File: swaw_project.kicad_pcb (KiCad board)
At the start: 2 copper layers, 68.6 x 53.3 mm, 22 parts, among them P1 Power, P2 Analog, P3 Digital, P4 Digital, P5 CONN_01X01, P6 CONN_01X01, P7 CONN_01X01, P8 CONN_01X01, Q1 2N7000, Q2 2N7000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

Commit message: First version of layout
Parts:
- moved R2 2.54 mm to (128.3, 94.6), turned to 0 degrees
- moved C4 1.78 mm to (135.8, 99.3)
- moved R5 0.43 mm to (135.1, 80.6), turned to 180 degrees
- moved C3 0.42 mm to (128.8, 108.2)
- moved R1 0.41 mm to (134.3, 94.6)
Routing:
- net +5V: track 0.00 -> 143.2 mm
- net GND: track 0.00 -> 122.4 mm, vias 0 -> 9
- net +3V3: track 0.00 -> 95.2 mm, vias 0 -> 6
- net /0(Rx): track 0.00 -> 25.1 mm
- net /1(Tx): track 0.00 -> 15.2 mm
- net /A5(SCL): track 0.00 -> 12.9 mm
- net Net-(HC-05_PIO1-Pad3): track 0.00 -> 12.8 mm
- net Net-(Q2-Pad1): track 0.00 -> 12.6 mm, vias 0 -> 1
- net /A4(SDA): track 0.00 -> 12.6 mm
- net Net-(Q1-Pad1): track 0.00 -> 12.4 mm, vias 0 -> 1
- net Net-(C4-Pad1): track 0.00 -> 7.66 mm, vias 0 -> 1
- net Net-(C3-Pad1): track 0.00 -> 3.93 mm, vias 0 -> 1

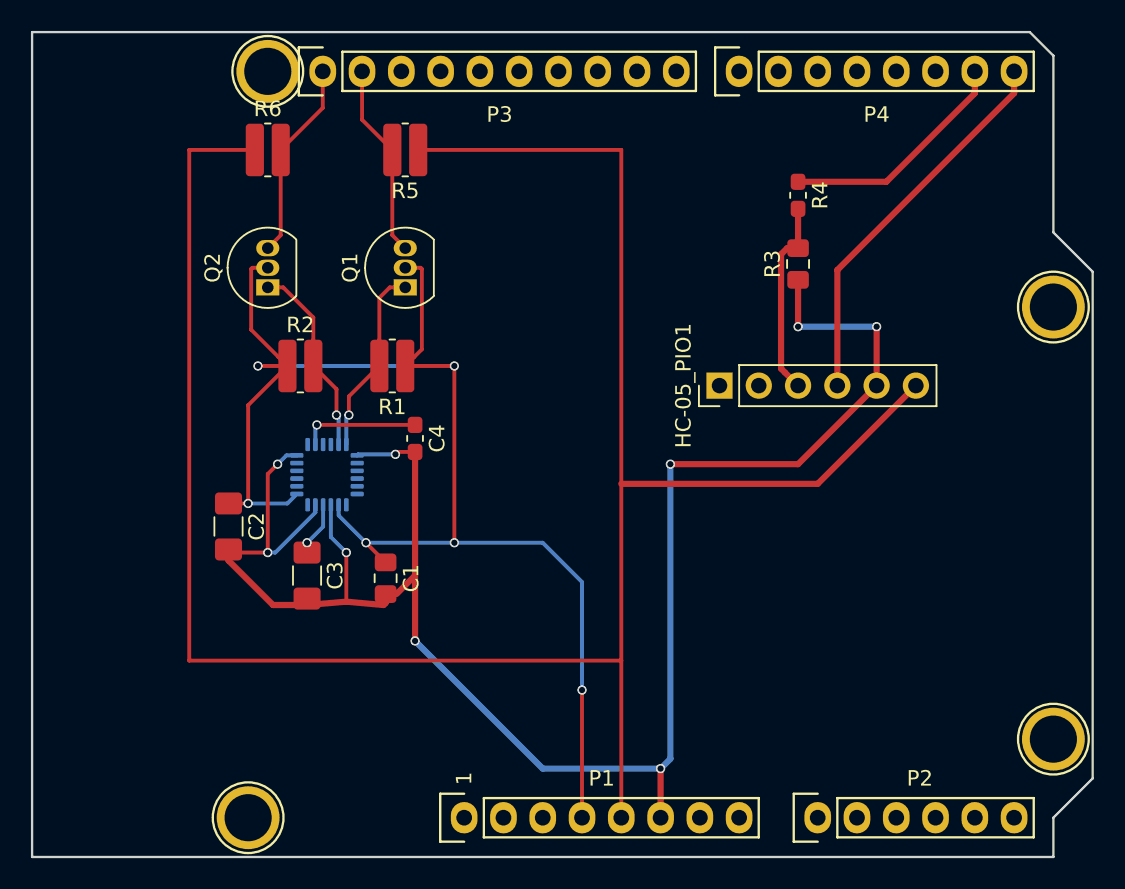
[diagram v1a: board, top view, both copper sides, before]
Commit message: Add files via upload
Removing right angles for paths
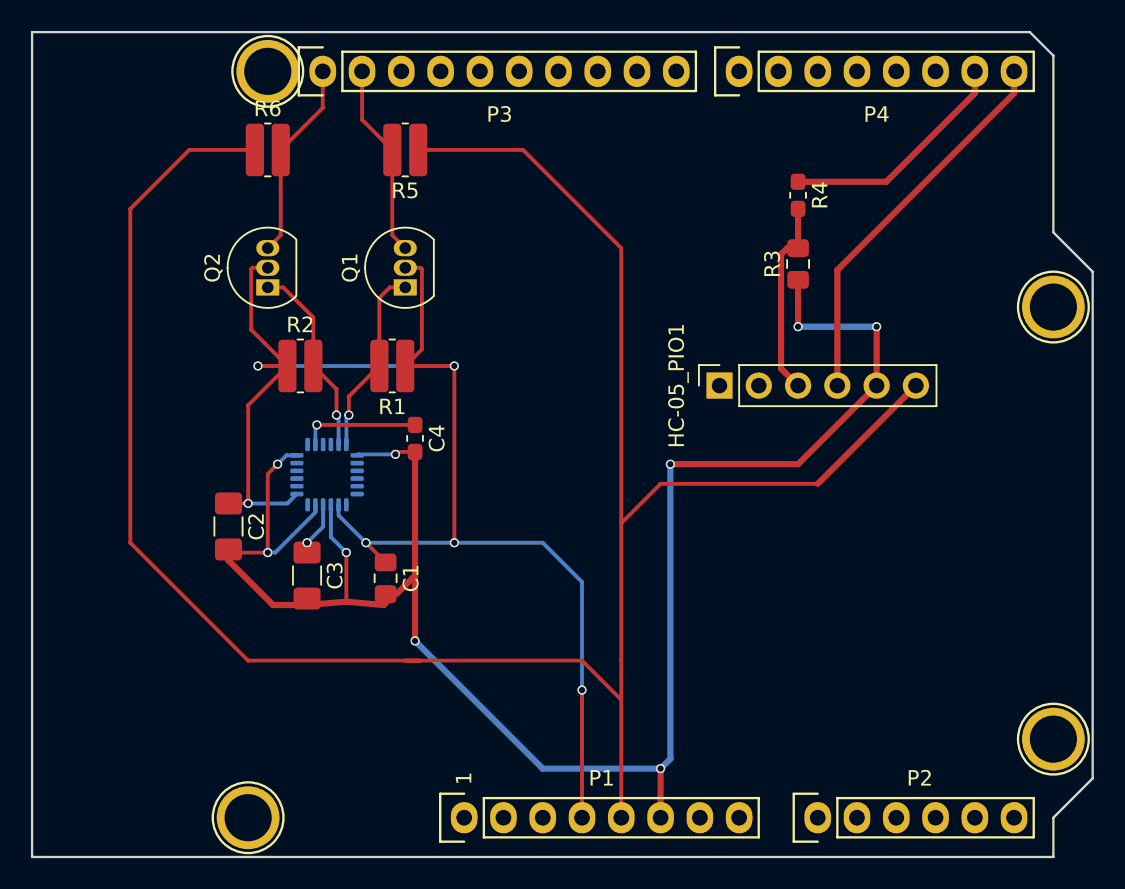
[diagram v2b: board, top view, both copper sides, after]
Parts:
- HC-05_PIO1: footprint Connector_PinHeader_2.54mm:PinHeader_1x06_P2.54mm_Vertical -> Connector_PinSocket_2.54mm:PinSocket_1x06_P2.54mm_Vertical
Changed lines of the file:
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@@
-(kicad_pcb (version 20171130) (host pcbnew 5.1.5)
+(kicad_pcb (version 20171130) (host pcbnew "(5.1.5)-3")
   (general
     (thickness 1.6)
     (drawings 27)
-    (tracks 135)
+    (tracks 142)
     (zones 0)
     (modules 22)
@@
   )
   (setup
-    (last_trace_width 0.4)
+    (last_trace_width 0.25)
     (user_trace_width 0.2)
     (user_trace_width 0.4)
@@
     (aux_axis_origin 110.998 126.365)
     (grid_origin 110.998 126.365)
-    (visible_elements FFFFFF7F)
+    (visible_elements 7FFFFFFF)
     (pcbplotparams
       (layerselection 0x00030_80000001)
@@
     (add_net "Net-(U1-Pad7)")
   )
+  (module Connector_PinSocket_2.54mm:PinSocket_1x06_P2.54mm_Vertical (layer F.Cu)
+    (at 155.448 95.885 90)
+    (descr "Through hole straight socket strip, 1x06, 2.54mm pitch, single row (from Kicad 4.0.7), script generated")
+    (tags "Through hole socket strip THT 1x06 2.54mm single row")
+    (fp_text reference HC-05_PIO1 (at 0 -2.77 90) (layer F.SilkS)
+      (effects (font (size 1 1) (thickness 0.15)))
+    )
+    (fp_text value Bluetooh_PIO (at 0 15.47 90) (layer F.Fab)
+      (effects (font (size 1 1) (thickness 0.15)))
+    )
+    (fp_text user %R (at 0 6.35) (layer F.Fab)
+      (effects (font (size 1 1) (thickness 0.15)))
+    )
+    (fp_line (start -1.8 14.45) (end -1.8 -1.8) (layer F.CrtYd) (width 0.05))
+    (fp_line (start 1.75 14.45) (end -1.8 14.45) (layer F.CrtYd) (width 0.05))
+    (fp_line (start 1.75 -1.8) (end 1.75 14.45) (layer F.CrtYd) (width 0.05))
+    (fp_line (start -1.8 -1.8) (end 1.75 -1.8) (layer F.CrtYd) (width 0.05))
+    (fp_line (start 0 -1.33) (end 1.33 -1.33) (layer F.SilkS) (width 0.12))
+    (fp_line (start 1.33 -1.33) (end 1.33 0) (layer F.SilkS) (width 0.12))
+    (fp_line (start 1.33 1.27) (end 1.33 14.03) (layer F.SilkS) (width 0.12))
+    (fp_line (start -1.33 14.03) (end 1.33 14.03) (layer F.SilkS) (width 0.12))
+    (fp_line (start -1.33 1.27) (end -1.33 14.03) (layer F.SilkS) (width 0.12))
+    (fp_line (start -1.33 1.27) (end 1.33 1.27) (layer F.SilkS) (width 0.12))
+    (fp_line (start -1.27 13.97) (end -1.27 -1.27) (layer F.Fab) (width 0.1))
+    (fp_line (start 1.27 13.97) (end -1.27 13.97) (layer F.Fab) (width 0.1))
+    (fp_line (start 1.27 -0.635) (end 1.27 13.97) (layer F.Fab) (width 0.1))
+    (fp_line (start 0.635 -1.27) (end 1.27 -0.635) (layer F.Fab) (width 0.1))
+    (fp_line (start -1.27 -1.27) (end 0.635 -1.27) (layer F.Fab) (width 0.1))
+    (pad 6 thru_hole oval (at 0 12.7 90) (size 1.7 1.7) (drill 1) (layers *.Cu *.Mask)
+      (net 3 +5V))
+    (pad 5 thru_hole oval (at 0 10.16 90) (size 1.7 1.7) (drill 1) (layers *.Cu *.Mask)
+      (net 4 GND))
+    (pad 4 thru_hole oval (at 0 7.62 90) (size 1.7 1.7) (drill 1) (layers *.Cu *.Mask)
+      (net 22 "/0(Rx)"))
+    (pad 3 thru_hole oval (at 0 5.08 90) (size 1.7 1.7) (drill 1) (layers *.Cu *.Mask)
+      (net 37 "Net-(HC-05_PIO1-Pad3)"))
+    (pad 2 thru_hole oval (at 0 2.54 90) (size 1.7 1.7) (drill 1) (layers *.Cu *.Mask)
+      (net 36 "Net-(HC-05_PIO1-Pad2)"))
+    (pad 1 thru_hole rect (at 0 0 90) (size 1.7 1.7) (drill 1) (layers *.Cu *.Mask)
+      (net 35 "Net-(HC-05_PIO1-Pad1)"))
+    (model ${KISYS3DMOD}/Connector_PinSocket_2.54mm.3dshapes/PinSocket_1x06_P2.54mm_Vertical.wrl
+      (at (xyz 0 0 0))
+      (scale (xyz 1 1 1))
+      (rotate (xyz 0 0 0))
+    )
+  )
   (module Socket_Arduino_Uno:Socket_Strip_Arduino_1x08 locked (layer F.Cu)
     (at 138.938 123.825)
@@
       (net 4 GND))
     (model ${KISYS3DMOD}/Capacitor_SMD.3dshapes/C_0603_1608Metric.wrl
-      (at (xyz 0 0 0))
-      (scale (xyz 1 1 1))
-      (rotate (xyz 0 0 0))
-    )
-  )
-  (module Connector_PinHeader_2.54mm:PinHeader_1x06_P2.54mm_Vertical (layer F.Cu)
-    (at 155.448 95.885 90)
-    (descr "Through hole straight pin header, 1x06, 2.54mm pitch, single row")
-    (tags "Through hole pin header THT 1x06 2.54mm single row")
-    (fp_text reference HC-05_PIO1 (at 0 -2.33 90) (layer F.SilkS)
-      (effects (font (size 1 1) (thickness 0.15)))
-    )
-    (fp_text value Bluetooh_PIO (at 0 15.03 90) (layer F.Fab)
-      (effects (font (size 1 1) (thickness 0.15)))
-    )
-    (fp_line (start -0.635 -1.27) (end 1.27 -1.27) (layer F.Fab) (width 0.1))
-    (fp_line (start 1.27 -1.27) (end 1.27 13.97) (layer F.Fab) (width 0.1))
-    (fp_line (start 1.27 13.97) (end -1.27 13.97) (layer F.Fab) (width 0.1))
-    (fp_line (start -1.27 13.97) (end -1.27 -0.635) (layer F.Fab) (width 0.1))
-    (fp_line (start -1.27 -0.635) (end -0.635 -1.27) (layer F.Fab) (width 0.1))
-    (fp_line (start -1.33 14.03) (end 1.33 14.03) (layer F.SilkS) (width 0.12))
-    (fp_line (start -1.33 1.27) (end -1.33 14.03) (layer F.SilkS) (width 0.12))
-    (fp_line (start 1.33 1.27) (end 1.33 14.03) (layer F.SilkS) (width 0.12))
-    (fp_line (start -1.33 1.27) (end 1.33 1.27) (layer F.SilkS) (width 0.12))
-    (fp_line (start -1.33 0) (end -1.33 -1.33) (layer F.SilkS) (width 0.12))
-    (fp_line (start -1.33 -1.33) (end 0 -1.33) (layer F.SilkS) (width 0.12))
-    (fp_line (start -1.8 -1.8) (end -1.8 14.5) (layer F.CrtYd) (width 0.05))
-    (fp_line (start -1.8 14.5) (end 1.8 14.5) (layer F.CrtYd) (width 0.05))
-    (fp_line (start 1.8 14.5) (end 1.8 -1.8) (layer F.CrtYd) (width 0.05))
-    (fp_line (start 1.8 -1.8) (end -1.8 -1.8) (layer F.CrtYd) (width 0.05))
-    (fp_text user %R (at 0 6.35) (layer F.Fab)
-      (effects (font (size 1 1) (thickness 0.15)))
-    )
-    (pad 1 thru_hole rect (at 0 0 90) (size 1.7 1.7) (drill 1) (layers *.Cu *.Mask)
-      (net 35 "Net-(HC-05_PIO1-Pad1)"))
-    (pad 2 thru_hole oval (at 0 2.54 90) (size 1.7 1.7) (drill 1) (layers *.Cu *.Mask)
-      (net 36 "Net-(HC-05_PIO1-Pad2)"))
-    (pad 3 thru_hole oval (at 0 5.08 90) (size 1.7 1.7) (drill 1) (layers *.Cu *.Mask)
-      (net 37 "Net-(HC-05_PIO1-Pad3)"))
-    (pad 4 thru_hole oval (at 0 7.62 90) (size 1.7 1.7) (drill 1) (layers *.Cu *.Mask)
-      (net 22 "/0(Rx)"))
-    (pad 5 thru_hole oval (at 0 10.16 90) (size 1.7 1.7) (drill 1) (layers *.Cu *.Mask)
-      (net 4 GND))
-    (pad 6 thru_hole oval (at 0 12.7 90) (size 1.7 1.7) (drill 1) (layers *.Cu *.Mask)
-      (net 3 +5V))
-    (model ${KISYS3DMOD}/Connector_PinHeader_2.54mm.3dshapes/PinHeader_1x06_P2.54mm_Vertical.wrl
       (at (xyz 0 0 0))
       (scale (xyz 1 1 1))
@@
   (gr_line (start 120.523 82.55) (end 120.523 93.98) (angle 90) (layer Dwgs.User) (width 0.15))
   (gr_line (start 104.648 82.55) (end 120.523 82.55) (angle 90) (layer Dwgs.User) (width 0.15))
-  (segment (start 135.9655 80.645) (end 149.098 80.645) (width 0.25) (layer F.Cu) (net 3))
-  (segment (start 121.158 113.665) (end 149.098 113.665) (width 0.25) (layer F.Cu) (net 3))
   (segment (start 125.4005 80.645) (end 121.158 80.645) (width 0.25) (layer F.Cu) (net 3))
-  (segment (start 121.158 80.645) (end 121.158 113.665) (width 0.25) (layer F.Cu) (net 3))
-  (segment (start 149.098 113.665) (end 149.098 123.825) (width 0.25) (layer F.Cu) (net 3))
   (segment (start 168.148 95.885) (end 161.798 102.235) (width 0.4) (layer F.Cu) (net 3))
-  (segment (start 149.098 80.645) (end 149.098 102.235) (width 0.25) (layer F.Cu) (net 3))
-  (segment (start 161.798 102.235) (end 149.098 102.235) (width 0.4) (layer F.Cu) (net 3))
-  (segment (start 149.098 102.235) (end 149.098 113.665) (width 0.25) (layer F.Cu) (net 3))
+  (segment (start 136.107998 113.665) (end 124.968 113.665) (width 0.25) (layer F.Cu) (net 3))
+  (segment (start 124.968 113.665) (end 117.348 106.045) (width 0.25) (layer F.Cu) (net 3))
+  (segment (start 117.348 106.045) (end 117.348 84.455) (width 0.25) (layer F.Cu) (net 3))
+  (segment (start 117.348 84.455) (end 121.158 80.645) (width 0.25) (layer F.Cu) (net 3))
+  (segment (start 142.748 80.645) (end 135.9655 80.645) (width 0.25) (layer F.Cu) (net 3))
+  (segment (start 149.098 86.995) (end 142.748 80.645) (width 0.25) (layer F.Cu) (net 3))
+  (segment (start 151.638 102.235) (end 149.098 104.775) (width 0.25) (layer F.Cu) (net 3))
+  (segment (start 161.798 102.235) (end 151.638 102.235) (width 0.25) (layer F.Cu) (net 3))
+  (segment (start 149.098 113.665) (end 149.098 104.775) (width 0.25) (layer F.Cu) (net 3))
+  (segment (start 149.098 104.775) (end 149.098 86.995) (width 0.25) (layer F.Cu) (net 3))
+  (segment (start 149.098 116.205) (end 149.098 123.825) (width 0.25) (layer F.Cu) (net 3))
+  (segment (start 149.098 116.205) (end 146.558 113.665) (width 0.25) (layer F.Cu) (net 3))
+  (segment (start 149.098 113.665) (end 149.098 116.205) (width 0.25) (layer F.Cu) (net 3))
+  (segment (start 146.558 113.665) (end 135.128 113.665) (width 0.25) (layer F.Cu) (net 3))
   (segment (start 123.698 107.1925) (end 123.698 106.48) (width 0.4) (layer F.Cu) (net 4))
   (segment (start 133.858 109.94) (end 133.858 109.365) (width 0.4) (layer F.Cu) (net 4))

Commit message: Adding changes to layout after review
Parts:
- added R7: 100Ω, Resistor_SMD:R_0603_1608Metric_Pad1.05x0.95mm_HandSolder, F.Cu at (164.3, 88.3)
- added R8: 100Ω, Resistor_SMD:R_0603_1608Metric_Pad1.05x0.95mm_HandSolder, F.Cu at (156.7, 88.0)
- C1: value 10nF -> 110nF
- Q1, Q2: value 2N7000 -> 2N7002; footprint Package_TO_SOT_THT:TO-92_Inline -> Package_TO_SOT_SMD:SOT-23
- U1: moved to F.Cu
- moved C3 8.64 mm to (131.3, 116.4), turned to 90 degrees
- moved C4 8.08 mm to (140.2, 106.0)
- moved C1 8.03 mm to (136.4, 116.0), turned to 90 degrees
- moved C2 7.41 mm to (127.5, 111.3)
- moved U1 7.40 mm to (133.9, 108.0), turned to 0 degrees
- moved R5 2.54 mm to (135.1, 83.2)
- moved R6 2.54 mm to (126.2, 83.2)
- moved R2 1.67 mm to (126.7, 94.6)
- moved Q1 1.27 mm to (135.1, 88.3)
- moved Q2 1.27 mm to (126.2, 88.3)
- moved R1 0.84 mm to (135.1, 94.6), turned to 0 degrees
- turned R3 to 270 degrees
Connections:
- HC-05_PIO1 pad 4: /0(Rx) -> Net-(HC-05_PIO1-Pad4)
- Q1 pad 1: Net-(Q1-Pad1) -> +3V3
- Q1 pad 2: +3V3 -> Net-(Q1-Pad2)
- Q2 pad 1: Net-(Q2-Pad1) -> +3V3
- Q2 pad 2: +3V3 -> Net-(Q2-Pad2)
- R1 pad 2: Net-(Q1-Pad1) -> Net-(Q1-Pad2)
- R2 pad 2: Net-(Q2-Pad1) -> Net-(Q2-Pad2)
- R3 pad 1: GND -> Net-(R3-Pad1)
- R3 pad 2: Net-(HC-05_PIO1-Pad3) -> GND
- R4 pad 1: /1(Tx) -> /0(Rx)
- R4 pad 2: Net-(HC-05_PIO1-Pad3) -> Net-(R3-Pad1)
- U1 pad 23: Net-(Q2-Pad1) -> Net-(Q2-Pad2)
- U1 pad 24: Net-(Q1-Pad1) -> Net-(Q1-Pad2)
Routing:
- net /A5(SCL): track 12.9 -> 88.4 mm, vias 0 -> 2
- net /A4(SDA): track 12.6 -> 70.3 mm, vias 0 -> 2
- net GND: track 122.4 -> 66.9 mm, vias 9 -> 2
- net Net-(Q1-Pad2): track 0.00 -> 21.7 mm, vias 0 -> 2
- net Net-(Q2-Pad2): track 0.00 -> 19.2 mm
- net +5V: track 143.5 -> 127.4 mm, vias 0 -> 4
- net Net-(Q2-Pad1): track 12.6 -> 0.00 mm, vias 1 -> 0
- net Net-(Q1-Pad1): track 12.4 -> 0.00 mm, vias 1 -> 0
- net Net-(HC-05_PIO1-Pad4): track 0.00 -> 7.12 mm
- net Net-(C3-Pad1): track 3.93 -> 10.4 mm, vias 1 -> 2
- net Net-(R3-Pad1): track 0.00 -> 6.35 mm
- net /0(Rx): track 25.1 -> 19.9 mm
- net Net-(HC-05_PIO1-Pad3): track 12.8 -> 8.42 mm
- net +3V3: track 95.2 -> 91.7 mm, vias 6 -> 3
- net /1(Tx): track 15.2 -> 17.8 mm, vias 0 -> 2
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
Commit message: Fixed tx/rx connection, added gnd planes and some vias
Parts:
- added C5: 1uF, Capacitor_SMD:C_1206_3216Metric_Pad1.42x1.75mm_HandSolder, F.Cu at (140.4, 113.7)
- C1: value 110nF -> 10nF
- R4: footprint Resistor_SMD:R_0603_1608Metric_Pad1.05x0.95mm_HandSolder -> Resistor_SMD:R_0805_2012Metric_Pad1.15x1.40mm_HandSolder
- moved C2 12.9 mm to (140.4, 111.1), turned to 0 degrees
- moved C1 10.1 mm to (128.1, 110.1)
- moved R8 5.28 mm to (160.5, 91.7)
- moved C4 4.91 mm to (136.0, 103.5), turned to 0 degrees
- moved R7 3.79 mm to (163.1, 91.8)
- moved C3 3.04 mm to (132.6, 113.7), turned to 180 degrees
- moved R3 1.45 mm to (161.6, 87.0), turned to 0 degrees
- moved R4 1.35 mm to (161.6, 84.5), turned to 180 degrees
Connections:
- R4 pad 1: /0(Rx) -> /1(Tx)
- R7 pad 1: /1(Tx) -> /0(Rx)
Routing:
- net /A5(SCL): track 88.4 -> 14.2 mm, vias 2 -> 0
- net GND: track 66.9 -> 9.37 mm, vias 2 -> 17
- net /A4(SDA): track 70.3 -> 12.9 mm, vias 2 -> 0
- net +5V: track 127.4 -> 90.3 mm, vias 4 -> 2
- net Net-(C3-Pad1): track 10.4 -> 3.73 mm, vias 2 -> 0
- net Net-(HC-05_PIO1-Pad3): track 8.42 -> 3.33 mm
- net Net-(C4-Pad1): track 7.63 -> 2.76 mm
- net /1(Tx): track 17.8 -> 13.8 mm, vias 2 -> 0
- net Net-(HC-05_PIO1-Pad4): track 7.12 -> 3.18 mm
- net Net-(Q1-Pad2): track 21.7 -> 18.4 mm
- net +3V3: track 91.7 -> 90.4 mm, vias 3 -> 2
- net /0(Rx): track 19.9 -> 20.4 mm
- added copper zone on B.Cu, net GND
- added copper zone on F.Cu, net GND
